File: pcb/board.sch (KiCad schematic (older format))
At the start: 16 parts, among them J1 0473460001, J4 Conn_01x06_Male, Q1 AO3400A, Q2 AO3400A, U1 CP2102N-A01-GQFN28, U2 NUF2042XV6T1G

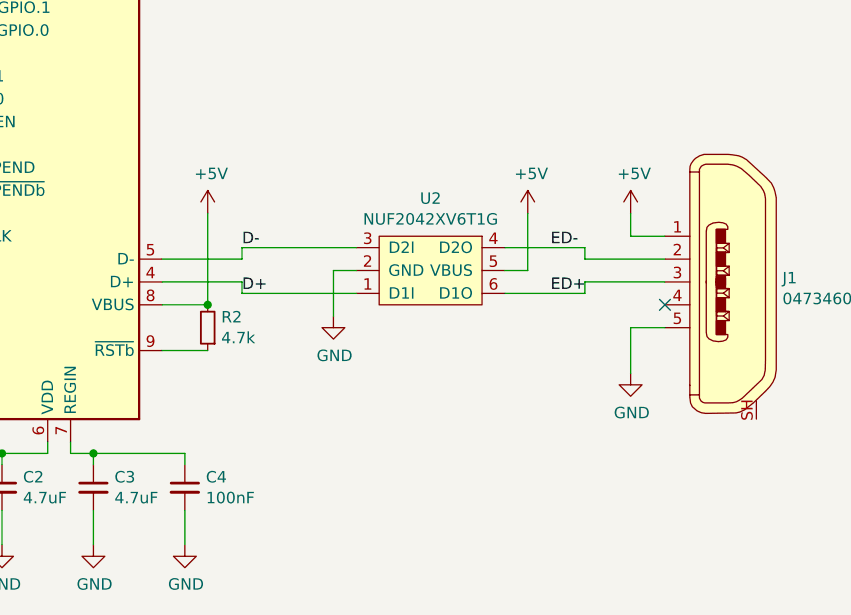
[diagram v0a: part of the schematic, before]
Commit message: fixed missing 5v connection and changed ESD diodes
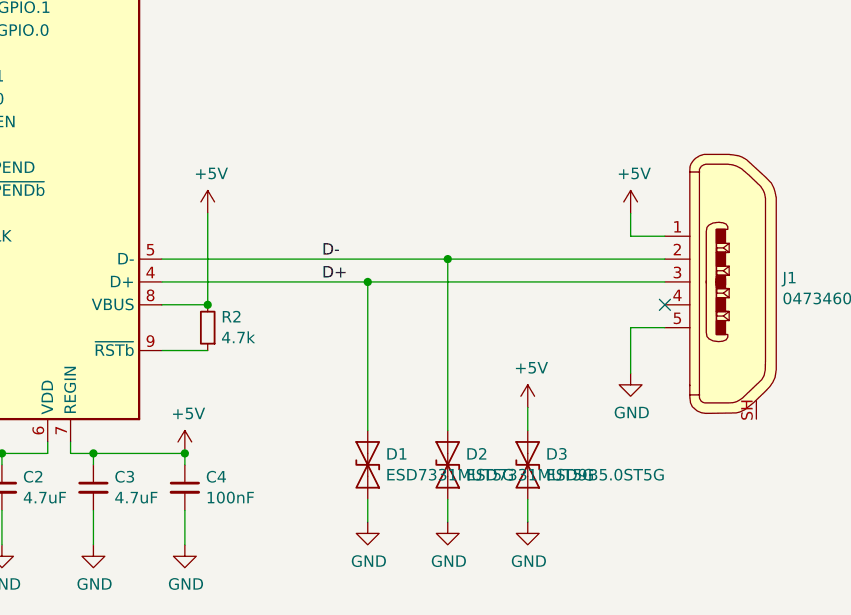
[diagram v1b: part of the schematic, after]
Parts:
- removed U2: NUF2042XV6T1G, parts:SOT-563, symbol parts:NUF2042XV6T1G
- added D1, D2: ESD7331MUT5G, Diode_SMD:D_0201_0603Metric, symbol Device:D_TVS
- added D3: ESD9B5.0ST5G, Diode_SMD:D_0402_1005Metric, symbol Device:D_TVS
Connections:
- net ED+ is gone; now on net D+: J1.3
- net ED- is gone; now on net D-: J1.2
- net +5V: now also C3.1, C4.1, U1.7 (REGIN), D3.1 (A1)
- net D+: now also D1.1 (A1)
- net D-: now also D2.1 (A1)
- net GND: now also D1.2 (A2), D2.2 (A2), D3.2 (A2)
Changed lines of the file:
@@
 $EndComp
-$Comp
-L parts:NUF2042XV6T1G U2
-U 1 1 5EB38317
-P 9050 4950
-F 0 "U2" H 9075 4635 50  0000 C CNN
-F 1 "NUF2042XV6T1G" H 9075 4726 50  0000 C CNN
-F 2 "parts:SOT-563" H 9050 4550 50  0001 C CNN
-F 3 "http://www.onsemi.com/pub/Collateral/NUF2030XV6-D.PDF" H 9050 4650 50  0001 C CNN
-	1    9050 4950
-	1    0    0    1
-$EndComp
-Wire Wire Line
-	10100 4900 9750 4900
-Wire Wire Line
-	9750 5000 9750 5050
-Wire Wire Line
-	9750 5050 9400 5050
-Wire Wire Line
-	9750 5000 10100 5000
-Wire Wire Line
-	9750 4900 9750 4850
-Wire Wire Line
-	9750 4850 9400 4850
 $Comp
 L power:+5V #PWR0101
@@
 	9950 4800 10100 4800
 $Comp
-L power:+5V #PWR0102
-U 1 1 5EB3C351
-P 9500 4700
-F 0 "#PWR0102" H 9500 4550 50  0001 C CNN
-F 1 "+5V" H 9515 4873 50  0000 C CNN
-F 2 "" H 9500 4700 50  0001 C CNN
-F 3 "" H 9500 4700 50  0001 C CNN
-	1    9500 4700
-	1    0    0    -1
-$EndComp
-Wire Wire Line
-	9500 4700 9500 4950
-Wire Wire Line
-	9500 4950 9400 4950
-$Comp
 L power:GND #PWR0103
 U 1 1 5EB3CE0D
@@
 	9950 5200 10100 5200
 NoConn ~ 10100 5100
-$Comp
-L power:GND #PWR0104
-U 1 1 5EB3DD55
-P 8650 5150
-F 0 "#PWR0104" H 8650 4900 50  0001 C CNN
-F 1 "GND" H 8655 4977 50  0000 C CNN
-F 2 "" H 8650 5150 50  0001 C CNN
-F 3 "" H 8650 5150 50  0001 C CNN
-	1    8650 5150
-	1    0    0    -1
-$EndComp
-Wire Wire Line
-	8650 5150 8650 4950
-Wire Wire Line
-	7900 4900 8250 4900
-Wire Wire Line
-	8250 4900 8250 4850
-Wire Wire Line
-	7900 5000 8250 5000
-Wire Wire Line
-	8250 5000 8250 5050
 $Comp
 L power:+5V #PWR0105
@@
 Wire Wire Line
 	5650 5400 6900 5400
-Wire Wire Line
-	8650 4950 8750 4950
-Wire Wire Line
-	8250 4850 8750 4850
-Wire Wire Line
-	8250 5050 8750 5050
-Text Label 8250 4850 0    50   ~ 0
+Text Label 8600 4900 0    50   ~ 0
 D-
-Text Label 8250 5050 0    50   ~ 0
+Text Label 8600 5000 0    50   ~ 0
 D+
-Text Label 9600 4850 0    50   ~ 0
-ED-
-Text Label 9600 5050 0    50   ~ 0
-ED+
+$Comp
+L Device:D_TVS D3
+U 1 1 5EC21336
+P 9500 5800
+F 0 "D3" V 9454 5879 50  0000 L CNN
+F 1 "ESD9B5.0ST5G" V 9545 5879 50  0000 L CNN
+F 2 "Diode_SMD:D_0402_1005Metric" H 9500 5800 50  0001 C CNN
+F 3 "~" H 9500 5800 50  0001 C CNN
+	1    9500 5800
+	0    1    1    0
+$EndComp
+$Comp
+L power:+5V #PWR0102
+U 1 1 5EC21A11
+P 9500 5550
+F 0 "#PWR0102" H 9500 5400 50  0001 C CNN
+F 1 "+5V" H 9515 5723 50  0000 C CNN
+F 2 "" H 9500 5550 50  0001 C CNN
+F 3 "" H 9500 5550 50  0001 C CNN
+	1    9500 5550
+	1    0    0    -1
+$EndComp
+$Comp
+L power:GND #PWR0104
+U 1 1 5EC21D5D
+P 9500 6050
+F 0 "#PWR0104" H 9500 5800 50  0001 C CNN
+F 1 "GND" H 9505 5877 50  0000 C CNN
+F 2 "" H 9500 6050 50  0001 C CNN
+F 3 "" H 9500 6050 50  0001 C CNN
+	1    9500 6050
+	1    0    0    -1
+$EndComp
+Wire Wire Line
+	9500 5950 9500 6050
+Wire Wire Line
+	9500 5550 9500 5650
+$Comp
+L power:+5V #PWR0112
+U 1 1 5EC24DBF
+P 8000 5750
+F 0 "#PWR0112" H 8000 5600 50  0001 C CNN
+F 1 "+5V" H 8015 5923 50  0000 C CNN
+F 2 "" H 8000 5750 50  0001 C CNN
+F 3 "" H 8000 5750 50  0001 C CNN
+	1    8000 5750
+	1    0    0    -1
+$EndComp
+Connection ~ 8000 5750
+$Comp
+L Device:D_TVS D2
+U 1 1 5EC2514C
+P 9150 5800
+F 0 "D2" V 9104 5879 50  0000 L CNN
+F 1 "ESD7331MUT5G" V 9195 5879 50  0000 L CNN
+F 2 "Diode_SMD:D_0201_0603Metric" H 9150 5800 50  0001 C CNN
+F 3 "~" H 9150 5800 50  0001 C CNN
+	1    9150 5800
+	0    1    1    0
+$EndComp
+$Comp
+L Device:D_TVS D1
+U 1 1 5EC254A5
+P 8800 5800
+F 0 "D1" V 8754 5879 50  0000 L CNN
+F 1 "ESD7331MUT5G" V 8845 5879 50  0000 L CNN
+F 2 "Diode_SMD:D_0201_0603Metric" H 8800 5800 50  0001 C CNN
+F 3 "~" H 8800 5800 50  0001 C CNN
+	1    8800 5800
+	0    1    1    0
+$EndComp
+$Comp
+L power:GND #PWR0113
+U 1 1 5EC272D3
+P 9150 6050
+F 0 "#PWR0113" H 9150 5800 50  0001 C CNN
+F 1 "GND" H 9155 5877 50  0000 C CNN
+F 2 "" H 9150 6050 50  0001 C CNN
+F 3 "" H 9150 6050 50  0001 C CNN
+	1    9150 6050
+	1    0    0    -1
+$EndComp
+Wire Wire Line
+	9150 5950 9150 6050
+$Comp
+L power:GND #PWR0114
+U 1 1 5EC288F9
+P 8800 6050
+F 0 "#PWR0114" H 8800 5800 50  0001 C CNN
+F 1 "GND" H 8805 5877 50  0000 C CNN
+F 2 "" H 8800 6050 50  0001 C CNN
+F 3 "" H 8800 6050 50  0001 C CNN
+	1    8800 6050
+	1    0    0    -1
+$EndComp
+Wire Wire Line
+	8800 5950 8800 6050
+Wire Wire Line
+	7900 5000 8800 5000
+Wire Wire Line
+	8800 5650 8800 5000
+Connection ~ 8800 5000
+Wire Wire Line
+	8800 5000 10100 5000
+Wire Wire Line
+	9150 5650 9150 4900
+Wire Wire Line
+	7900 4900 9150 4900
+Connection ~ 9150 4900
+Wire Wire Line
+	9150 4900 10100 4900
 $EndSCHEMATC
